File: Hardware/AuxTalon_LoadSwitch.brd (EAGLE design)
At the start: 70 x 35 mm, 89 parts, among them J1 CONN_AUX_M12_REMOTE, J2 CONN_AUX_M12_REMOTE, J3 CONN_AUX_M12_REMOTE, J4 CONN_TALON_REMOTE, U1 ADS1115, U11 MCP23018QFN, U16 MAX9064, U17 MAX9064, U18 SN74AUP1T87, U19 MAX9064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

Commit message: v1.3 Layout
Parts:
- moved C9 59.6 mm to (59.1, 11.9)
- moved C10 39.2 mm to (35.1, 13.6)
- moved R13 32.2 mm to (14.2, 15.5), turned to 90 degrees
- moved C11 24.3 mm to (11.0, 12.1)
- moved S1 1.27 mm to (17.5, 15.5)
- moved R23 0.46 mm to (38.9, 16.6)
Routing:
- net GND: track 413.9 -> 430.4 mm, vias 16 -> 17
- net D2: track 10.4 -> 14.3 mm
- net D1: track 10.0 -> 13.5 mm
- net C1: track 56.6 -> 60.0 mm
- net 3V3: track 296.7 -> 299.9 mm
- net OD2: track 5.59 -> 8.49 mm
- net OD3: track 6.62 -> 9.36 mm
- net OD1: track 7.22 -> 9.66 mm
- net C2: track 57.0 -> 58.0 mm
- net 5V: track 140.9 -> 141.9 mm
- net VPORT1_IN: track 18.1 -> 17.2 mm

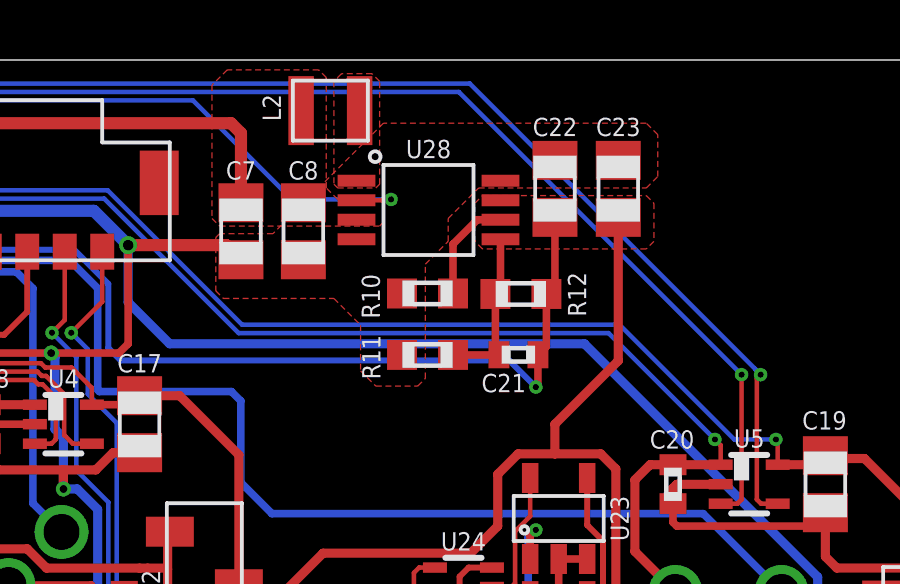
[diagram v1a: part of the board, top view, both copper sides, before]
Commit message: Updated part vals for v1.3
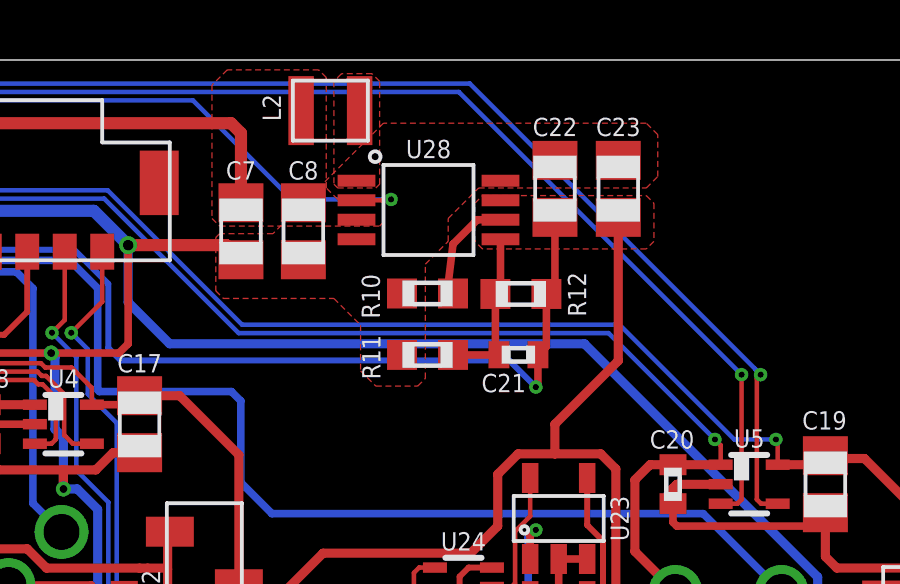
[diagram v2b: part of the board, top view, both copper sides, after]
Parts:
- C10, C11, C9: value (none) -> 47nF
- C2, C3, C4: value 4.7uF -> 0.1uF
- R13, R23, R24: value (none) -> 100k
- R16, R17, R18, R3, R4, R5: value 100k -> 10k

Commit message: Updates for modified BoM
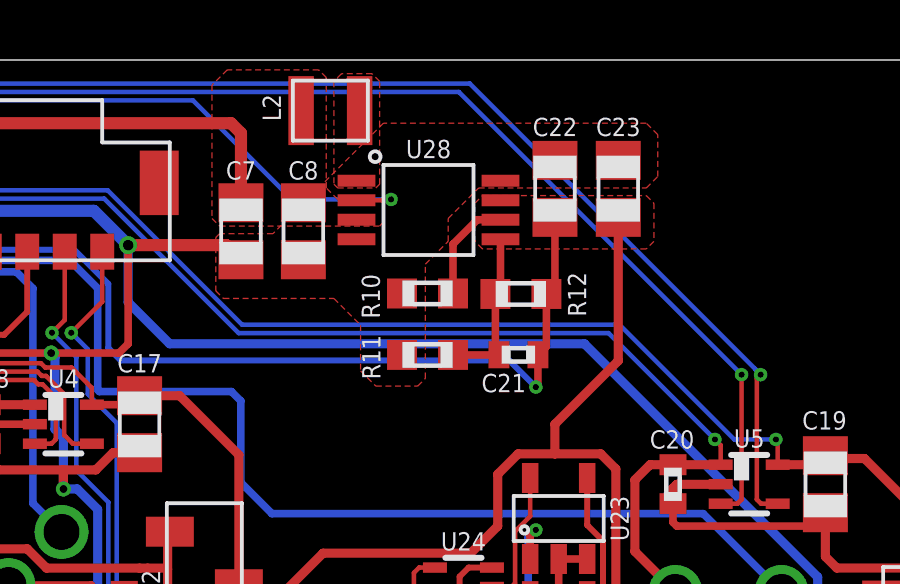
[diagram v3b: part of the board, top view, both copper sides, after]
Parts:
- R10: value 68k -> 100k
- U6: value 24AA02SOT23 -> AT24MAC602SOT23
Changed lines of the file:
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@@
 <attribute name="NAME" x="57.404" y="11.589" size="0.6096" layer="25" font="vector" ratio="15" rot="R180" align="center"/>
 </element>
-<element name="U6" library="bschulz" package="SOT23-5" value="24AA02SOT23" x="28.35" y="23.27" smashed="yes" rot="R270">
-<attribute name="DIGIKEY" value="24AA025E64T-I/OTCT-ND" x="30.35" y="23.27" size="1.27" layer="27" font="vector" ratio="15" rot="R270" display="off"/>
-<attribute name="DISP" value="24AA025E64" x="30.35" y="23.27" size="1.27" layer="27" font="vector" ratio="15" rot="R270" display="off"/>
+<element name="U6" library="bschulz" package="SOT23-5" value="AT24MAC602SOT23" x="28.35" y="23.27" smashed="yes" rot="R270">
+<attribute name="DIGIKEY" value="AT24MAC602-STUM-TCT-ND" x="30.35" y="23.27" size="1.27" layer="27" font="vector" ratio="15" rot="R270" display="off"/>
+<attribute name="DISP" value="AT24MAC602" x="30.35" y="23.27" size="1.27" layer="27" font="vector" ratio="15" rot="R270" display="off"/>
 <attribute name="MF" value="Microchip" x="30.35" y="23.27" size="1.27" layer="27" font="vector" ratio="15" rot="R270" display="off"/>
-<attribute name="MOUSER" value="24AA025E64T-I/OTCT-ND" x="30.35" y="23.27" size="1.27" layer="27" font="vector" ratio="15" rot="R270" display="off"/>
-<attribute name="MPN" value="24AA025E64T-I/OT" x="30.35" y="23.27" size="1.27" layer="27" font="vector" ratio="15" rot="R270" display="off"/>
+<attribute name="MPN" value="AT24MAC602-STUM-T" x="30.35" y="23.27" size="1.27" layer="27" font="vector" ratio="15" rot="R270" display="off"/>
 <attribute name="NAME" x="28.35" y="21.365" size="0.6096" layer="25" font="vector" ratio="15" align="center"/>
 <attribute name="VALUE" x="28.477" y="20.984" size="0.6096" layer="27" font="vector" ratio="15" align="center"/>
@@
 <attribute name="VALUE" x="43.432" y="29.291" size="0.6096" layer="27" font="vector" ratio="15" rot="R270" align="center"/>
 </element>
-<element name="R10" library="bschulz_passives" package="R0603" value="68k" x="48.967" y="27.217" smashed="yes">
-<attribute name="DIGIKEY" value="" x="48.967" y="27.217" size="1.778" layer="27" display="off"/>
+<element name="R10" library="bschulz_passives" package="R0603" value="100k" x="48.967" y="27.217" smashed="yes">
+<attribute name="DIGIKEY" value="311-100KHRCT-ND" x="48.967" y="27.217" size="1.778" layer="27" display="off"/>
 <attribute name="MF" value="Yageo" x="48.967" y="27.217" size="1.778" layer="27" display="off"/>
-<attribute name="MPN" value="RC0402FR-07100KL" x="48.967" y="27.217" size="1.778" layer="27" display="off"/>
+<attribute name="MPN" value="RC0603FR-07100KL" x="48.967" y="27.217" size="1.778" layer="27" display="off"/>
 <attribute name="NAME" x="47.078" y="27.123" size="0.6096" layer="25" font="vector" ratio="15" rot="R90" align="center"/>
 <attribute name="VALUE" x="48.967" y="26.201" size="0.6096" layer="27" font="vector" ratio="15" align="center"/>
@@
 <wire x1="53.215" y1="31.655" x2="55.326" y2="31.655" width="0" layer="19" extent="1-1"/>
 <wire x1="51.4" y1="30.975" x2="53.215" y2="31.655" width="0" layer="19" extent="1-1"/>
-<wire x1="48.317" y1="27.217" x2="51.4" y2="30.975" width="0" layer="19" extent="1-1"/>
-<wire x1="48.118" y1="25.169" x2="48.317" y2="27.217" width="0" layer="19" extent="1-1"/>
-<wire x1="46.6" y1="29.025" x2="48.317" y2="27.217" width="0" layer="19" extent="1-1"/>
+<wire x1="48.117" y1="27.217" x2="51.4" y2="30.975" width="0" layer="19" extent="1-1"/>
+<wire x1="48.118" y1="25.169" x2="48.117" y2="27.217" width="0" layer="19" extent="1-1"/>
+<wire x1="46.6" y1="29.025" x2="48.117" y2="27.217" width="0" layer="19" extent="1-1"/>
 <wire x1="44.829" y1="28.341" x2="46.6" y2="29.025" width="0" layer="19" extent="1-1"/>
 <wire x1="42.749" y1="28.341" x2="44.829" y2="28.341" width="0" layer="19" extent="1-1"/>
@@
 <contactref element="R10" pad="2"/>
 <contactref element="U28" pad="6"/>
-<wire x1="49.617" y1="27.217" x2="49.817" y2="28.862" width="0.254" layer="1"/>
+<wire x1="49.817" y1="27.217" x2="49.817" y2="28.862" width="0.254" layer="1"/>
 <wire x1="50.63" y1="29.675" x2="51.4" y2="29.675" width="0.254" layer="1"/>
 <wire x1="49.817" y1="28.862" x2="50.63" y2="29.675" width="0.254" layer="1"/>

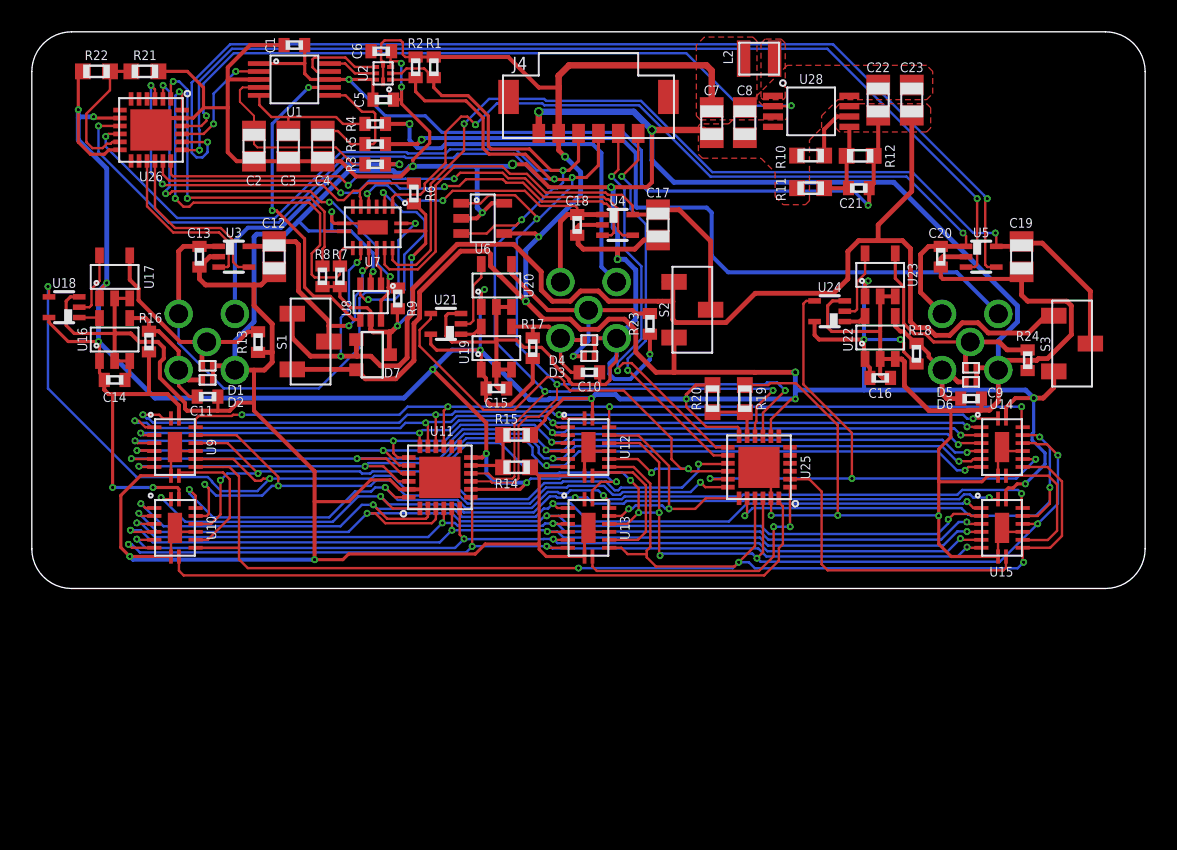
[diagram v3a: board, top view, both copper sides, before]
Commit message: v1.4 Updates
Updated schematic and layout, boards sent to fab
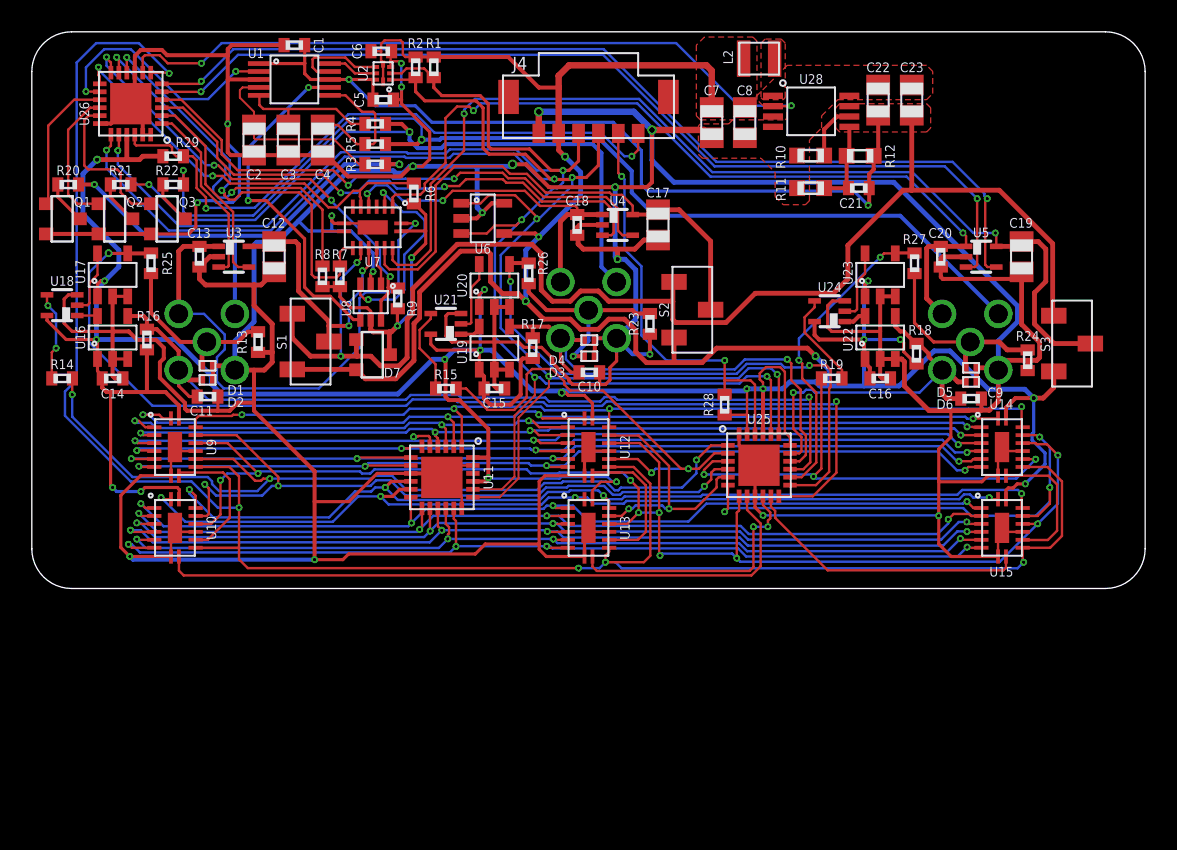
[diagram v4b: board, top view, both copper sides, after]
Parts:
- added Q1, Q2, Q3: 2N7002, bschulz:SOT23-3
- added R25, R26, R27: 1k, bschulz_passives:R0402
- added R28, R29: 100k, bschulz_passives:R0402
- R14: value 82k -> 1k; device bschulz_passives:R0603 -> bschulz_passives:R0402
- R15, R19: value 62k -> 1k; device bschulz_passives:R0603 -> bschulz_passives:R0402
- R20: value 82k -> 10k; device bschulz_passives:R0603 -> bschulz_passives:R0402
- R21: device bschulz_passives:R0603 -> bschulz_passives:R0402
- R22: value 150k -> 10k; device bschulz_passives:R0603 -> bschulz_passives:R0402
- U11, U25, U26: value MCP23018QFN -> PCAL9535AQFN
- moved R20 42.7 mm to (2.29, 25.4), turned to 0 degrees
- moved R14 29.1 mm to (1.91, 13.2), turned to 0 degrees
- moved R22 8.59 mm to (8.89, 25.4), turned to 0 degrees
- moved R21 7.27 mm to (5.59, 25.4), turned to 0 degrees
- moved R19 5.61 mm to (50.3, 13.2), turned to 180 degrees
- moved R15 5.32 mm to (26.0, 12.6)
- moved U26 2.08 mm to (6.22, 30.5), turned to 180 degrees
- moved C2 0.38 mm to (14.0, 28.2)
- moved C3 0.38 mm to (16.1, 28.2)
- moved C4 0.38 mm to (18.3, 28.2)
- moved U18 0.18 mm to (1.91, 17.8)
- moved R16 0.18 mm to (7.24, 15.7)
- moved U16 0.18 mm to (5.08, 15.8)
- moved U17 0.18 mm to (5.08, 19.7)
- moved C14 0.16 mm to (5.08, 13.2)
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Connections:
- new net ACTRL1: Q1.1, U26.15
- new net ACTRL2: Q2.1, U26.16
- new net ACTRL3: Q3.1, U26.17
- new net D1_SENSE: R25.2, U17.4, U25.12
- new net D2_SENSE: R26.2, U20.4, U25.13
- new net D3_SENSE: R27.2, U23.4, U25.14
- new net N$15: Q1.3, R20.1
- new net N$17: R15.1, U21.4
- new net N$19: R19.1, U24.4
- net !OVF1: now also U25.8; no longer U25.24
- net !OVF2: now also U25.10; no longer U25.1
- net !OVF3: now also U25.11; no longer U25.2
- net !PORT1_FAULT: now also U26.1; no longer U26.15
- net !PORT2_FAULT: now also U26.3; no longer U26.17
- net !PORT3_FAULT: now also U26.5; no longer U26.19
- net !RST: now also U26.7; no longer U25.21
- net 3V3: now also R28.2, R29.2, U11.21, U11.24, U25.18, U25.21, U25.23, U26.21; no longer R15.2, R20.2, R22.2, U11.12, U11.8, U25.12, U25.8, U26.12, U26.8
- net 5V_EN: now also U26.8; no longer U26.22
- net ADC_INT: now also U26.14; no longer U26.21
- net AIN1: now also R20.2
- net AIN2: now also R21.2
- net AIN3: now also R22.2
- net C0: now also U11.1; no longer U11.15
- net C1: now also U11.2; no longer U11.16
- net C10: now also U11.12; no longer U11.2
- net C11: now also U11.13; no longer U11.3
- net C12: now also U11.14; no longer U11.4
- net C13: now also U11.15; no longer U11.5
- net C14: now also U11.16; no longer U11.6
- net C15: now also U11.17; no longer U11.7
- net C2: now also U11.3; no longer U11.17
- net C3: now also U11.4; no longer U11.18
- net C4: now also U11.5; no longer U11.19
- net C5: now also U11.6; no longer U11.20
- net C6: now also U11.7; no longer U11.21
- net C7: now also U11.8; no longer U11.22
- net C8: now also U11.10; no longer U11.24
- net C9: now also U11.11; no longer U11.1
- net COUNT_EN1: now also U25.4; no longer U25.18
- net COUNT_EN2: now also U25.5; no longer U25.19
- net COUNT_EN3: now also U25.6; no longer U25.20
- net D1: now also R25.1; no longer U17.4
- net D2: now also R26.1; no longer U20.4
- net D3: now also R27.1; no longer U23.4
- net GND: now also Q1.2, Q2.2, Q3.2, U11.18, U11.9, U25.24, U25.9, U26.18, U26.24, U26.9; no longer R14.1, R19.1, R21.1, U25.23
- net GPIOA: now also R29.1, U26.22; no longer U25.14
- net GPIOB: now also R28.1, U25.22; no longer U25.13
- net LOAD: now also U25.7; no longer U25.22
- net MUX_EN: now also U26.13; no longer U26.3
- net MUX_SEL0: now also U26.10; no longer U26.24
- net MUX_SEL1: now also U26.11; no longer U26.1
- net MUX_SEL2: now also U26.12; no longer U26.2
- net N$14: now also Q2.3, R21.1; no longer R21.2, R22.1, U26.11
- net N$16: now also R14.1, U18.4; no longer R19.2, R20.1, U25.11
- net N$7: now also Q3.3, R22.1; no longer R14.2, R15.1, U11.11
- net OD1: now also U25.15
- net OD2: now also U25.16
- net OD3: now also U25.17
- net OUT1: now also R14.2, U25.1; no longer U18.4, U25.15
- net OUT2: now also R15.2, U25.2; no longer U21.4, U25.16
- net OUT3: now also R19.2, U25.3; no longer U24.4, U25.17
- net PORT1_EN: now also U26.2; no longer U26.16
- net PORT2_EN: now also U26.4; no longer U26.18
- net PORT3_EN: now also U26.6; no longer U26.20
- net SCL: now also U11.19, U25.19, U26.19; no longer U11.9, U25.9, U26.9
- net SDA: now also U11.20, U25.20, U26.20; no longer U11.10, U25.10, U26.10
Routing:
- net D1_SENSE: track 0.00 -> 66.7 mm, vias 0 -> 2
- net OD1: track 9.66 -> 56.4 mm, vias 0 -> 1
- net D2_SENSE: track 0.00 -> 36.3 mm, vias 0 -> 2
- net !RST: track 91.8 -> 126.6 mm, vias 3 -> 5
- net OD2: track 8.49 -> 32.2 mm, vias 0 -> 1
- net AIN2: track 23.6 -> 44.1 mm, vias 1 -> 2
- net D3_SENSE: track 0.00 -> 19.8 mm, vias 0 -> 2
- net AIN3: track 46.8 -> 66.2 mm, vias 1 -> 2
- net GPIOA: track 24.9 -> 40.2 mm
- net OD3: track 9.36 -> 24.1 mm, vias 0 -> 1
- net GND: track 430.4 -> 441.8 mm, vias 17 -> 18
- net AIN1: track 17.8 -> 29.2 mm, vias 1 -> 2
- net ACTRL3: track 0.00 -> 9.88 mm
- net ACTRL1: track 0.00 -> 8.88 mm
- net ACTRL2: track 0.00 -> 8.80 mm
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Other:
- board text added: "Talon - Aux v1.4 Bobby Schulz"
- board text removed: "Talon - Aux v1.3 - LS Bobby Schulz"

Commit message: Updates for v1.5
- Changed load switch
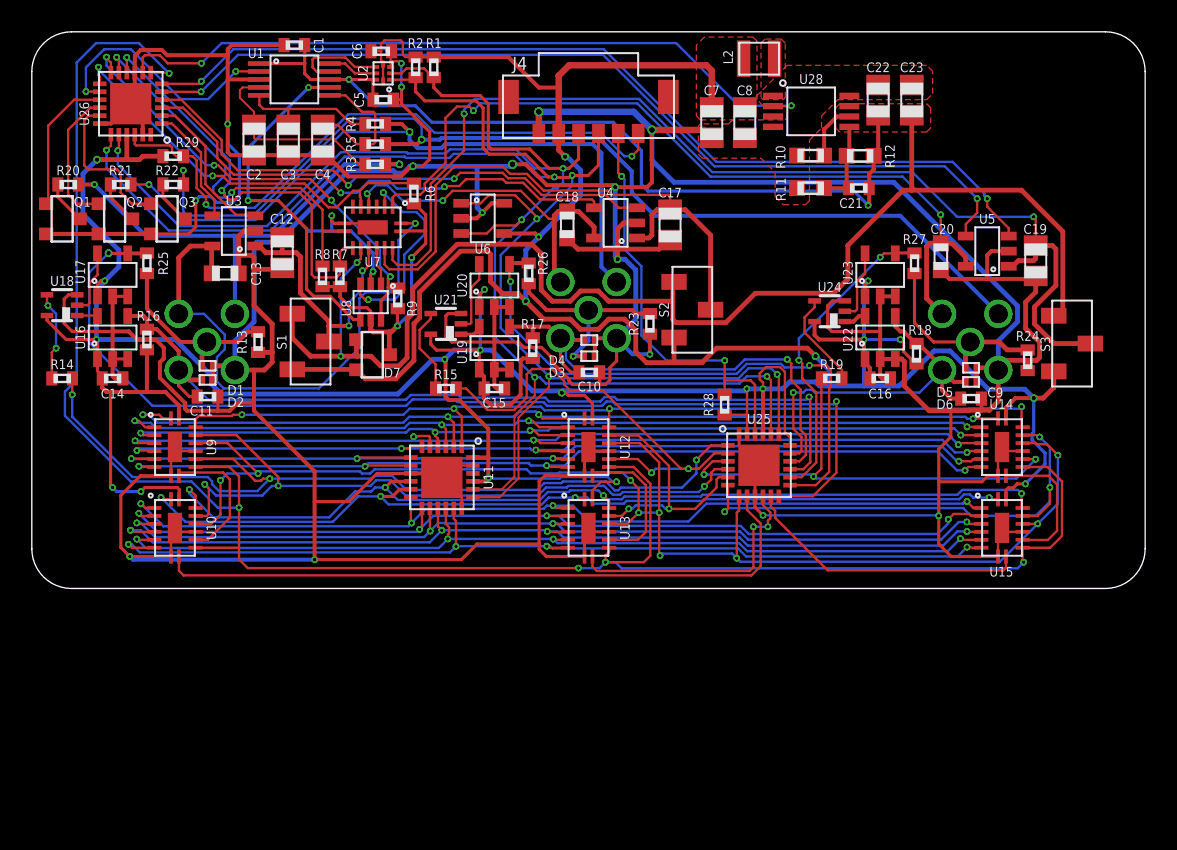
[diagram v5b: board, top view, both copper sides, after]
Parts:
- C13, C18, C20: value 0.1uF -> 1uF; device bschulz_passives:C0402 -> bschulz_passives:C0603
- U3, U4, U5: value TPS22944 -> MIC2090-2; device bschulz:DCK_R-PDSO-G5 -> bschulz:SOT23-5
- moved C13 1.93 mm to (12.2, 19.8), turned to 0 degrees
- moved U3 1.62 mm to (12.7, 22.5), turned to 90 degrees
- moved C19 0.92 mm to (63.1, 20.6)
- moved C17 0.76 mm to (40.1, 22.9)
- moved C18 0.63 mm to (33.7, 22.9)
- moved C12 0.57 mm to (15.7, 21.1)
- moved U5 0.52 mm to (60.1, 21.2), turned to 90 degrees
- moved R25 0.25 mm to (7.24, 20.4)
- moved U4 0.18 mm to (36.7, 23.0), turned to 90 degrees
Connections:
- net !PORT1_FAULT: now also U3.4; no longer U3.3
- net !PORT2_FAULT: now also U4.4; no longer U4.3
- net !PORT3_FAULT: now also U5.4; no longer U5.3
- net PORT1_EN: now also U3.3; no longer U3.4
- net PORT2_EN: now also U4.3; no longer U4.4
- net PORT3_EN: now also U5.3; no longer U5.4
- net VPORT1_IN: now also U3.1; no longer U3.5
- net VPORT1_OUT: now also U3.5; no longer U3.1
- net VPORT2_IN: now also U4.1; no longer U4.5
- net VPORT2_OUT: now also U4.5; no longer U4.1
- net VPORT3_IN: now also U5.1; no longer U5.5
- net VPORT3_OUT: now also U5.5; no longer U5.1
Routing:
- net VPORT3_IN: track 63.9 -> 68.3 mm
- net !PORT1_FAULT: track 11.7 -> 7.60 mm
- net GND: track 441.8 -> 445.7 mm
- net VPORT2_IN: track 33.6 -> 37.3 mm
- net !PORT2_FAULT: track 34.9 -> 31.7 mm
- net PORT1_EN: track 12.7 -> 9.89 mm
- net !PORT3_FAULT: track 60.9 -> 58.6 mm
- net PORT3_EN: track 61.7 -> 59.7 mm
- net 5V: track 138.8 -> 140.2 mm
- net PORT2_EN: track 35.2 -> 34.0 mm
- net VPORT1_OUT: track 34.4 -> 35.5 mm
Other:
- board text added: "Talon - Aux v1.5 Bobby Schulz"
- board text removed: "Talon - Aux v1.4 Bobby Schulz"
